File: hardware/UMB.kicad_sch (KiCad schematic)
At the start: 0 parts

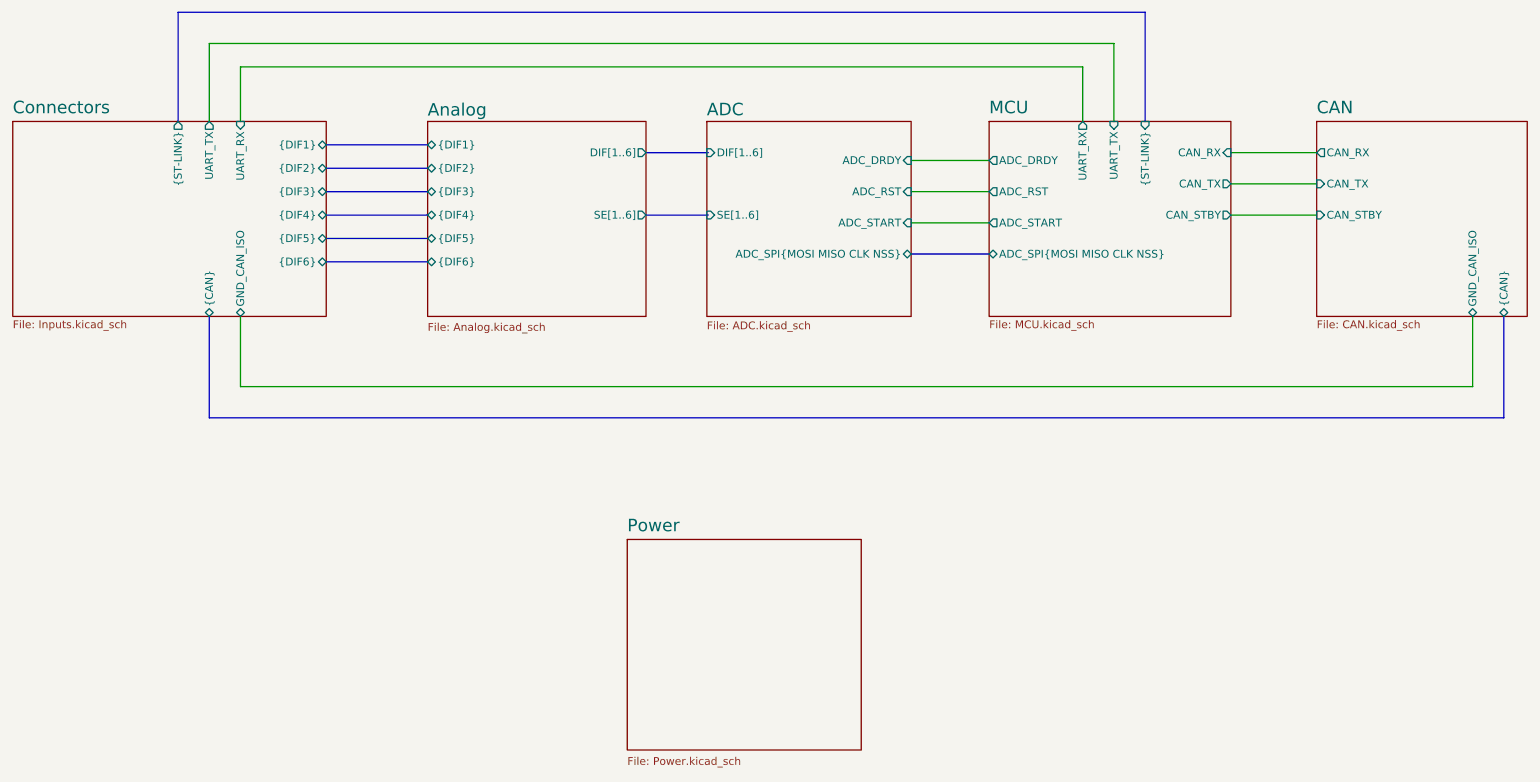
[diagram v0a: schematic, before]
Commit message: Fixed pinout errors & changed branch name
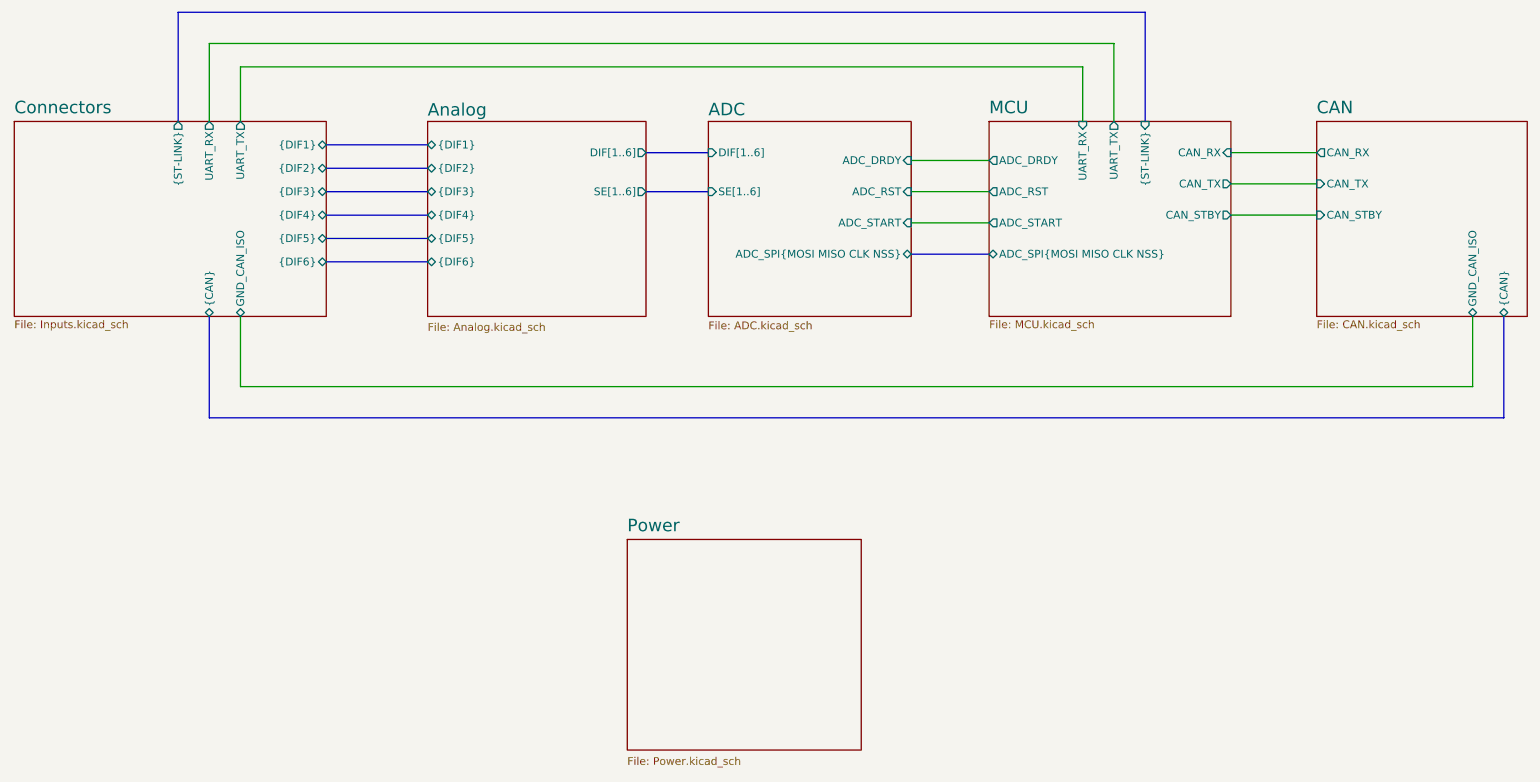
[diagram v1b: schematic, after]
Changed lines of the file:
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@@
 (kicad_sch
-	(version 20250114)
+	(version 20260306)
 	(generator "eeschema")
-	(generator_version "9.0")
+	(generator_version "10.0")
 	(paper "A4")
 	(title_block
@@
 		(comment 1 "Reviewer:")
 	)
-	(bus_alias "ST-LINK"
-		(members "SWDIO" "SWCLK" "NRST")
+	(wire
+		(pts
+			(xy 63.5 34.29) (xy 63.5 43.18)
+		)
+		(stroke
+			(width 0)
+			(type default)
+		)
 	)
 	(bus
@@
 	(wire
 		(pts
-			(xy 63.5 43.18) (xy 63.5 34.29)
-		)
-		(stroke
-			(width 0)
-			(type default)
-		)
-	)
-	(wire
-		(pts
 			(xy 63.5 86.36) (xy 264.16 86.36)
 		)
@@
 		)
 	)
+	(wire
+		(pts
+			(xy 58.42 30.48) (xy 58.42 43.18)
+		)
+		(stroke
+			(width 0)
+			(type default)
+		)
+	)
 	(bus
 		(pts
@@
 	(bus
 		(pts
-			(xy 129.54 58.42) (xy 139.7 58.42)
+			(xy 129.54 54.61) (xy 139.7 54.61)
 		)
 		(stroke
@@
 	(wire
 		(pts
-			(xy 58.42 30.48) (xy 58.42 43.18)
-		)
-		(stroke
-			(width 0)
-			(type default)
-		)
-	)
-	(wire
-		(pts
 			(xy 172.72 59.69) (xy 185.42 59.69)
 		)
@@
 	)
 	(sheet
-		(at 139.446 43.18)
-		(size 33.274 31.75)
+		(at 139.7 43.18)
+		(size 33.02 31.75)
 		(exclude_from_sim no)
 		(in_bom yes)
@@
 		)
 		(fill
-			(color 0 0 0 0.0000)
+			(color 0 0 0 0)
 		)
 		(property "Sheetname" "ADC"
-			(at 139.446 42.418 0)
+			(at 139.7 42.418 0)
+			(show_name no)
+			(do_not_autoplace no)
 			(effects
 				(font
@@
 		)
 		(property "Sheetfile" "ADC.kicad_sch"
-			(at 139.446 75.692 0)
+			(at 139.7 75.692 0)
+			(show_name no)
+			(do_not_autoplace no)
 			(effects
 				(font
@@
 		)
 		(pin "DIF[1..6]" input
-			(at 139.446 48.26 180)
+			(at 139.7 48.26 180)
 			(effects
 				(font
@@
 		)
 		(pin "SE[1..6]" input
-			(at 139.446 58.42 180)
+			(at 139.7 54.61 180)
 			(effects
 				(font
@@
 	)
 	(sheet
-		(at 26.416 43.18)
-		(size 51.054 31.75)
+		(at 26.67 43.18)
+		(size 50.8 31.75)
 		(exclude_from_sim no)
 		(in_bom yes)
@@
 		)
 		(fill
-			(color 0 0 0 0.0000)
+			(color 0 0 0 0)
 		)
 		(property "Sheetname" "Connectors"
-			(at 26.416 42.0874 0)
+			(at 26.67 42.0874 0)
+			(show_name no)
+			(do_not_autoplace no)
 			(effects
 				(font
@@
 		)
 		(property "Sheetfile" "Inputs.kicad_sch"
-			(at 26.416 75.5146 0)
+			(at 26.67 75.5146 0)
+			(show_name no)
+			(do_not_autoplace no)
 			(effects
 				(font
@@
 			)
 		)
-		(pin "UART_RX" input
+		(pin "UART_RX" output
+			(at 58.42 43.18 90)
+			(effects
+				(font
+					(size 1.27 1.27)
+				)
+				(justify right)
+			)
+		)
+		(pin "UART_TX" output
 			(at 63.5 43.18 90)
-			(effects
-				(font
-					(size 1.27 1.27)
-				)
-				(justify right)
-			)
-		)
-		(pin "UART_TX" output
-			(at 58.42 43.18 90)
 			(effects
 				(font
@@
 		)
 		(fill
-			(color 0 0 0 0.0000)
+			(color 0 0 0 0)
 		)
 		(property "Sheetname" "Power"
 			(at 126.492 110.1594 0)
+			(show_name no)
+			(do_not_autoplace no)
 			(effects
 				(font
@@
 		(property "Sheetfile" "Power.kicad_sch"
 			(at 126.492 146.6346 0)
+			(show_name no)
+			(do_not_autoplace no)
 			(effects
 				(font
@@
 		)
 		(fill
-			(color 0 0 0 0.0000)
+			(color 0 0 0 0)
 		)
 		(property "Sheetname" "MCU"
 			(at 185.42 42.0874 0)
+			(show_name no)
+			(do_not_autoplace no)
 			(effects
 				(font
@@
 		(property "Sheetfile" "MCU.kicad_sch"
 			(at 185.42 75.5146 0)
+			(show_name no)
+			(do_not_autoplace no)
 			(effects
 				(font
@@
 		(property "Field2" ""
 			(at 185.42 43.18 0)
+			(show_name no)
+			(do_not_autoplace no)
 			(effects
 				(font
@@
 			)
 		)
-		(pin "UART_RX" output
+		(pin "UART_RX" input
 			(at 200.66 43.18 90)
 			(effects
@@
 			)
 		)
-		(pin "UART_TX" input
+		(pin "UART_TX" output
 			(at 205.74 43.18 90)
 			(effects
@@
 		)
 		(fill
-			(color 0 0 0 0.0000)
+			(color 0 0 0 0)
 		)
 		(property "Sheetname" "Analog"
 			(at 93.98 42.4684 0)
+			(show_name no)
+			(do_not_autoplace no)
 			(effects
 				(font
@@
 		(property "Sheetfile" "Analog.kicad_sch"
 			(at 93.98 75.946 0)
+			(show_name no)
+			(do_not_autoplace no)
 			(effects
 				(font
@@
 		)
 		(pin "SE[1..6]" output
-			(at 129.54 58.42 0)
+			(at 129.54 54.61 0)
 			(effects
 				(font
@@
 		)
 		(fill
-			(color 0 0 0 0.0000)
+			(color 0 0 0 0)
 		)
 		(property "Sheetname" "CAN"
 			(at 238.76 42.0874 0)
+			(show_name no)
+			(do_not_autoplace no)
 			(effects
 				(font
@@
 		(property "Sheetfile" "CAN.kicad_sch"
 			(at 238.76 75.5146 0)
-			(effects
-				(font
+			(show_name no)
+			(do_not_autoplace no)
+			(effects
+				(font
